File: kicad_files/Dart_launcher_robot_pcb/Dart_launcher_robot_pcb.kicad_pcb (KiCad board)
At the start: 2 copper layers, 108.5 x 85.8 mm, 23 parts, among them J1 Conn_01x10_Pin, J10 Conn_01x08_Pin, J11 Conn_01x10_Pin, J12 Conn_01x04_Pin, J13 Conn_01x03_Pin, J14 Conn_01x03_Pin, J15 Conn_01x04_Pin, J16 Conn_01x03_Pin, J17 Conn_01x03_Pin, J18 Conn_01x03_Pin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

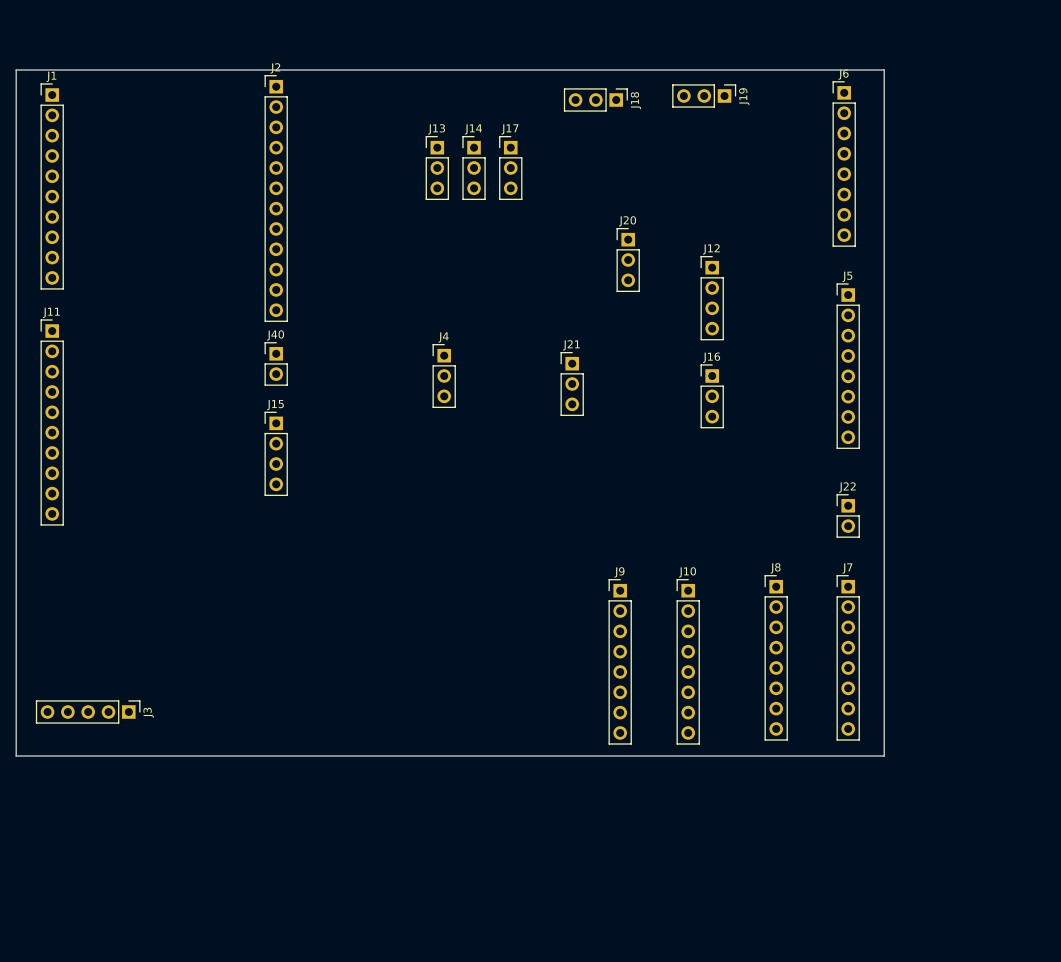
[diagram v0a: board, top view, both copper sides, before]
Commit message: pcb design and changes to the pitch_yaw_launcher_code
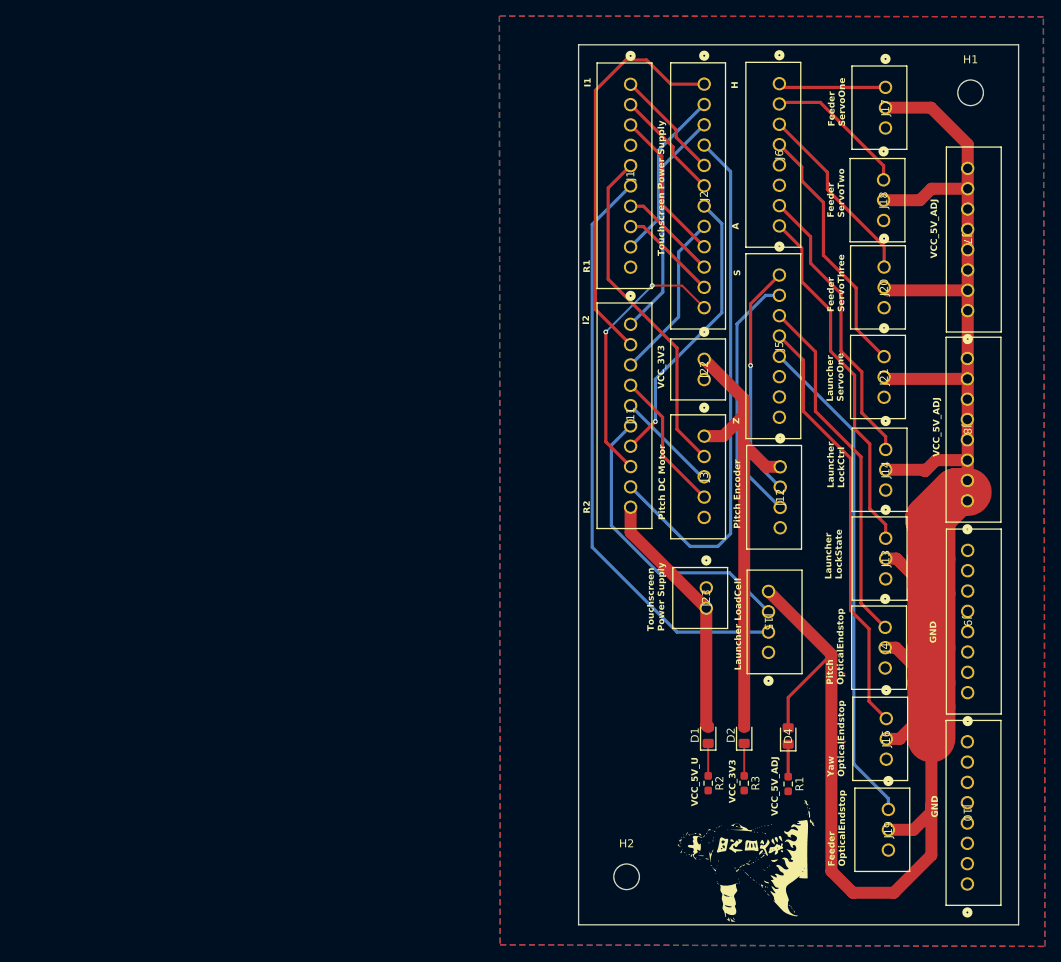
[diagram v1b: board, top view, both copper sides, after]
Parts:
- removed J40: Conn_01x02_Pin, Connector_PinHeader_2.54mm:PinHeader_1x02_P2.54mm_Vertical
- added D1: LED, LED_SMD:LED_0805_2012Metric_Pad1.15x1.40mm_HandSolder, F.Cu at (155.5, 120.9)
- added D2: LED, LED_SMD:LED_0805_2012Metric_Pad1.15x1.40mm_HandSolder, F.Cu at (160.0, 120.9)
- added D4: LED, LED_SMD:LED_0805_2012Metric_Pad1.15x1.40mm_HandSolder, F.Cu at (165.5, 121.0)
- added G***: LOGO, Images:fourth_hokage, F.Cu at (160.8, 136.3)
- added G***: LOGO, Images:monica_smaller, B.Cu at (150.5, 126.6)
- added H1: MountingHole, MountingHole:MountingHole_3.2mm_M3, F.Cu at (188.3, 40.6)
- added H2: MountingHole, MountingHole:MountingHole_3.2mm_M3, F.Cu at (145.3, 138.6)
- added J23: 705430036, footprints_3:CONN_SDA-70543-xxxx_02_MOL, F.Cu at (155.3, 102.5)
- added R1: R_Small_US, Resistor_SMD:R_0603_1608Metric_Pad0.98x0.95mm_HandSolder, F.Cu at (165.5, 127.0)
- added R2: R_Small_US, Resistor_SMD:R_0603_1608Metric_Pad0.98x0.95mm_HandSolder, F.Cu at (155.5, 126.9)
- added R3: R_Small_US, Resistor_SMD:R_0603_1608Metric_Pad0.98x0.95mm_HandSolder, F.Cu at (160.0, 126.9)
- J1, J11: value Conn_01x10_Pin -> 705430009; footprint Connector_PinHeader_2.54mm:PinHeader_1x10_P2.54mm_Vertical -> footprints_3:CONN_SDA-70543-xxxx_10_MOL
- J10, J5, J6, J7, J8, J9: value Conn_01x08_Pin -> 705430042; footprint Connector_PinHeader_2.54mm:PinHeader_1x08_P2.54mm_Vertical -> footprints_3:CONN_SDA-70543-xxxx_08_MOL
- J12, J15: value Conn_01x04_Pin -> 705430038; footprint Connector_PinHeader_2.54mm:PinHeader_1x04_P2.54mm_Vertical -> footprints_3:CONN_SDA-70543-xxxx_04_MOL
- J13, J14, J16, J17, J18, J19, J20, J21, J4: value Conn_01x03_Pin -> 705430037; footprint Connector_PinHeader_2.54mm:PinHeader_1x03_P2.54mm_Vertical -> footprints_3:CONN_SDA-70543-xxxx_03_MOL
- J2: value Conn_01x12_Pin -> 705430011; footprint Connector_PinHeader_2.54mm:PinHeader_1x12_P2.54mm_Vertical -> footprints_3:CONN_SDA-70543-xxxx_12_MOL
- J22: value Conn_01x02_Pin -> 705430036; footprint Connector_PinHeader_2.54mm:PinHeader_1x02_P2.54mm_Vertical -> footprints_3:CONN_SDA-70543-xxxx_02_MOL
- J3: value Conn_01x05_Pin -> 705430004; footprint Connector_PinHeader_2.54mm:PinHeader_1x05_P2.54mm_Vertical -> footprints:CONN_SDA-70543-xxxx_05_MOL
- moved J19 91.5 mm to (178.0, 130.2), turned to 90 degrees
- moved J3 79.8 mm to (155.0, 83.5), turned to 90 degrees
- moved J13 74.3 mm to (177.7, 96.3), turned to 90 degrees
- moved J1 72.3 mm to (145.8, 39.5), turned to 90 degrees
- moved J11 72.3 mm to (145.8, 69.5), turned to 90 degrees
- moved J15 67.9 mm to (163.0, 110.5), turned to -90 degrees
- moved J4 64.7 mm to (177.6, 107.4), turned to 90 degrees
- moved J14 63.8 mm to (177.7, 85.2), turned to 90 degrees
- moved J2 53.5 mm to (155.0, 39.5), turned to 90 degrees
- moved J10 50.6 mm to (187.9, 139.5), turned to -90 degrees
- moved J16 48.0 mm to (177.8, 118.8), turned to 90 degrees
- moved J17 47.4 mm to (177.7, 39.9), turned to 90 degrees
- moved J9 45.3 mm to (187.9, 115.6), turned to -90 degrees
- moved J21 39.0 mm to (177.5, 73.6), turned to 90 degrees
- moved J7 37.6 mm to (187.9, 67.8), turned to -90 degrees
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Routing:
- net VCC_5V_ADJ: track 0.00 -> 243.0 mm
- net PC4: track 0.00 -> 73.6 mm
- net PI9: track 0.00 -> 66.2 mm
- net PI5: track 0.00 -> 62.3 mm
- net 3V3: track 0.00 -> 59.8 mm
- net PA3: track 0.00 -> 53.4 mm
- net PE4: track 0.00 -> 50.0 mm
- net PI0: track 0.00 -> 44.6 mm
- net PA2: track 0.00 -> 44.4 mm
- net PC3: track 0.00 -> 42.5 mm
- net PC0: track 0.00 -> 37.6 mm
- net PH12: track 0.00 -> 36.0 mm
- net PC1: track 0.00 -> 35.7 mm, vias 0 -> 1
- net PA4: track 0.00 -> 34.5 mm, vias 0 -> 2
- net PA1: track 0.00 -> 32.0 mm
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- added copper zone on B.Cu, net GND
- added copper zone on F.Cu, net GND
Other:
- board size 108.5 x 85.8 mm -> 55 x 110 mm
- board text added: "A"
- board text added: "Feeder OpticalEndstop"
- board text added: "Feeder ServoOne"
- board text added: "Feeder ServoThree"
- board text added: "Feeder ServoTwo"
- board text added: "GND"
- board text added: "H"
- board text added: "I1"
- board text added: "I2"
- board text added: "Launcher LoadCell"
- board text added: "Launcher LockCtrl"
- board text added: "Launcher LockState"
- board text added: "Launcher ServoOne"
- board text added: "Pitch DC Motor"
- board text added: "Pitch Encoder"
- board text added: "Pitch OpticalEndstop"
- board text added: "R1"
- board text added: "R2"
- board text added: "S"
- board text added: "Touchscreen Power Supply"
- board text added: "VCC_3V3"
- board text added: "VCC_5V_ADJ"
- board text added: "VCC_5V_U"
- board text added: "Yaw OpticalEndstop"
- board text added: "Z"
